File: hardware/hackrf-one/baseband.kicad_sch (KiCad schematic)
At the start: 136 parts, among them P14 XCVR_CLKOUT, P15 INTR, P16 CLKIN, P18 OEB, P2 CLKOUT, P36 VAA, P37 SCL, P38 SDA, P39 SSP1_SCK, P40 SSP1_MOSI, P41 SSP1_MISO, P53 CS_XCVR, P54 CS_AD, P55 TXENABLE, P56 RXENABLE, P57 XTAL2, P58 GCK1, P59 GCK2, P60 SGPIO_CLK, P61 DA0, P62 DA7, P63 DD0, P64 DD9, P65 DA4, P66 DD5, P67 RSSI, P83 GND, P84 GND, P85 GND, P86 GND, P87 GND, P88 GND, P89 GND, P9 BASEBAND, P90 GND, P91 GND, P92 GND, Q3 MOSFET_P, T3 RX_BALUN, T4 TX_BALUN, U17 MAX2837, U18 MAX5864, U19 SI5351C, X1 GSG-XTAL4PIN

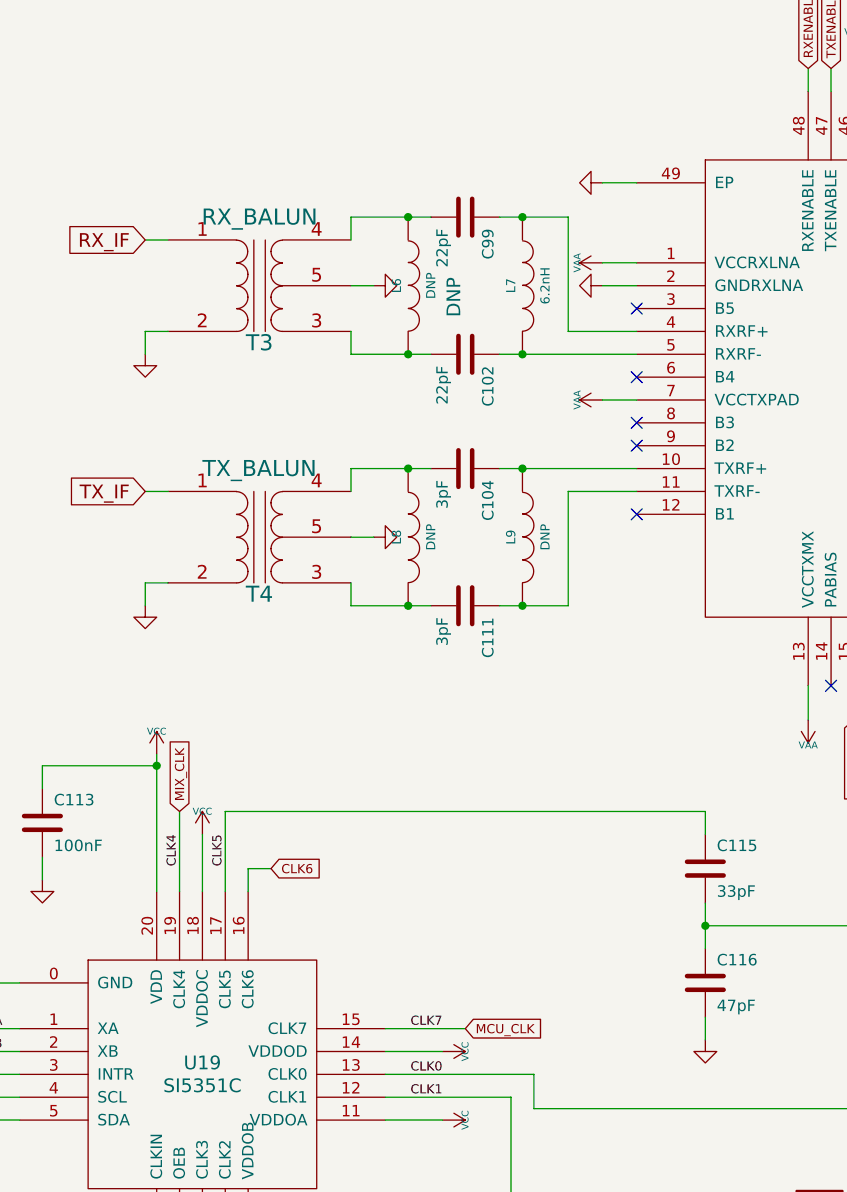
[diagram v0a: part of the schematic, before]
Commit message: Attempts to resolve wierd legacy ERC errors
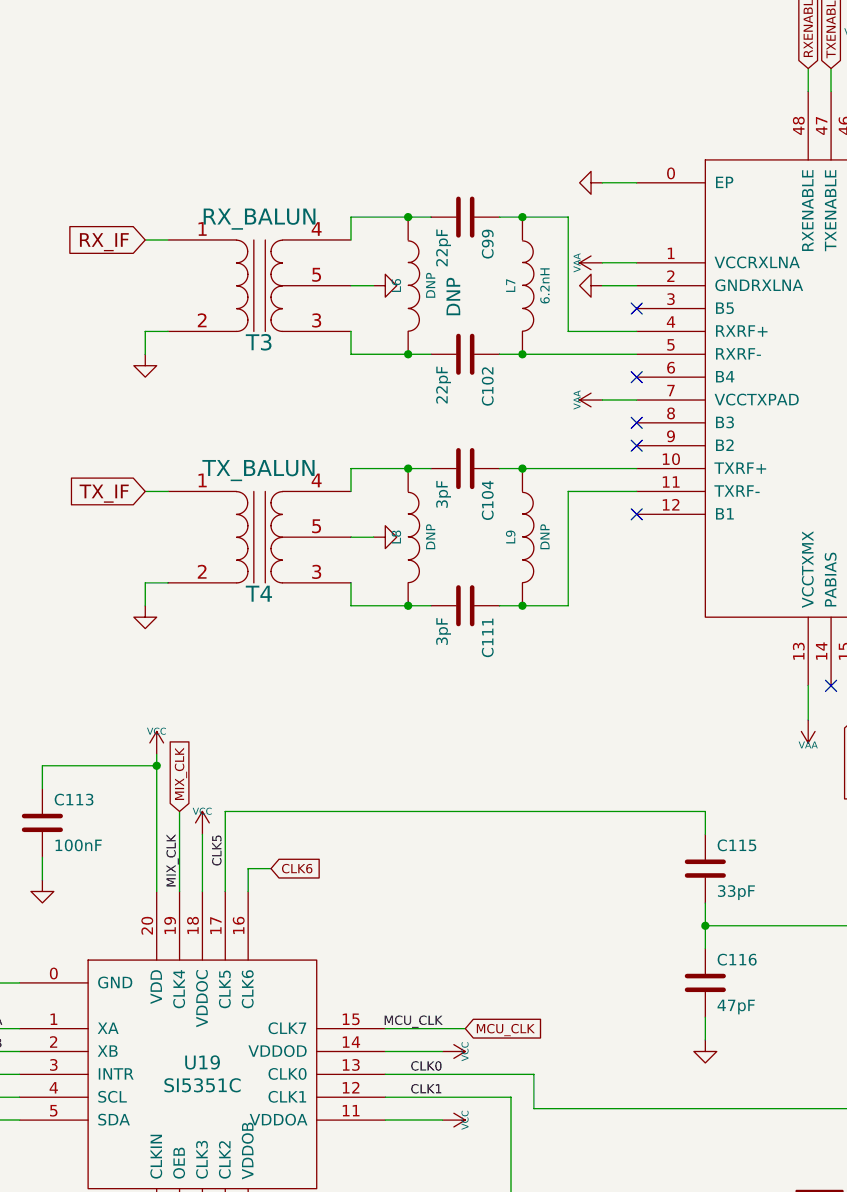
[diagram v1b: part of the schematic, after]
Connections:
- net GND: now also U17.0 (EP); no longer U17.49 (EP)
